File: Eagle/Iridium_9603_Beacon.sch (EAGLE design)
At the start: 100 parts, among them CON4 uFL, J1 SS4-10-3.50-X-D, Q1 DMG3415U-7, Q2 DMG3415U-7, Q3 DMG3415U-7, Q4 DMG3415U-7, Q5 2N2222, U1 MCP111T-240E/TT, U2 SPX3819-3.3, U3 LTC3225EDDB#TRMPBF, U4 MPL3115A2LGA8, U5 ATSAMD21G18_QFN, U6 MAX-M8, U7 LT1634-1,25BMCMS8, X1 32.768

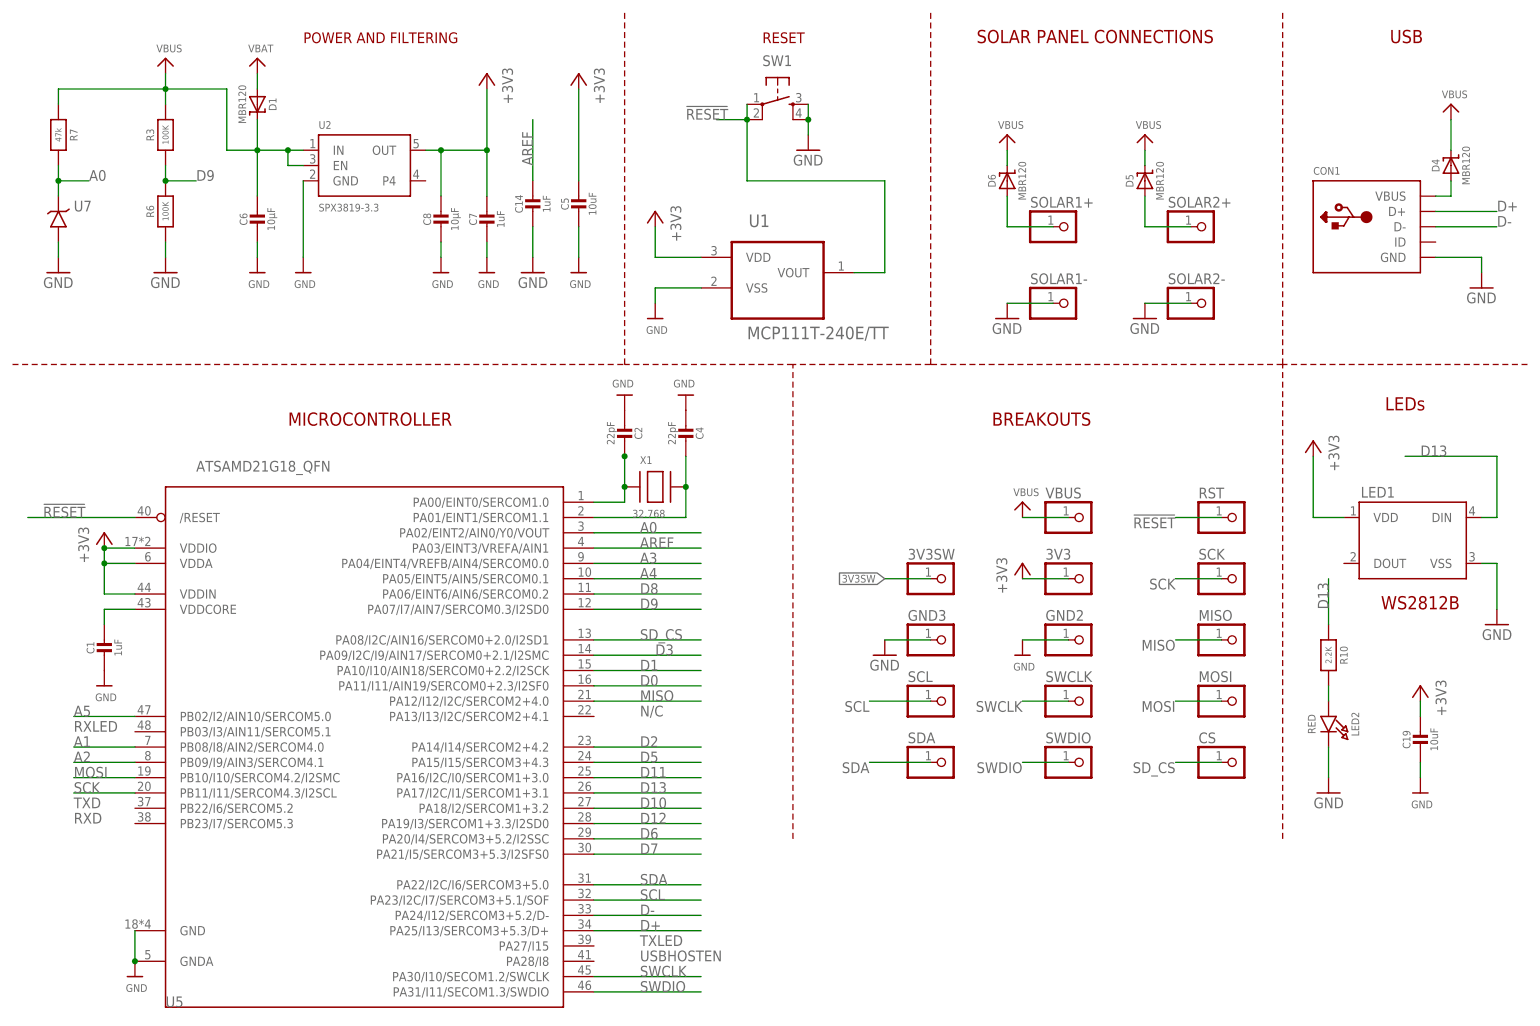
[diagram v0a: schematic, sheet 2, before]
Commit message: Corrected the zero width polygons
Corrected the zero width polygons in the micro USB connector that were causing problems for OSH Park. Thanks go to Paul Loewen @ usask.ca
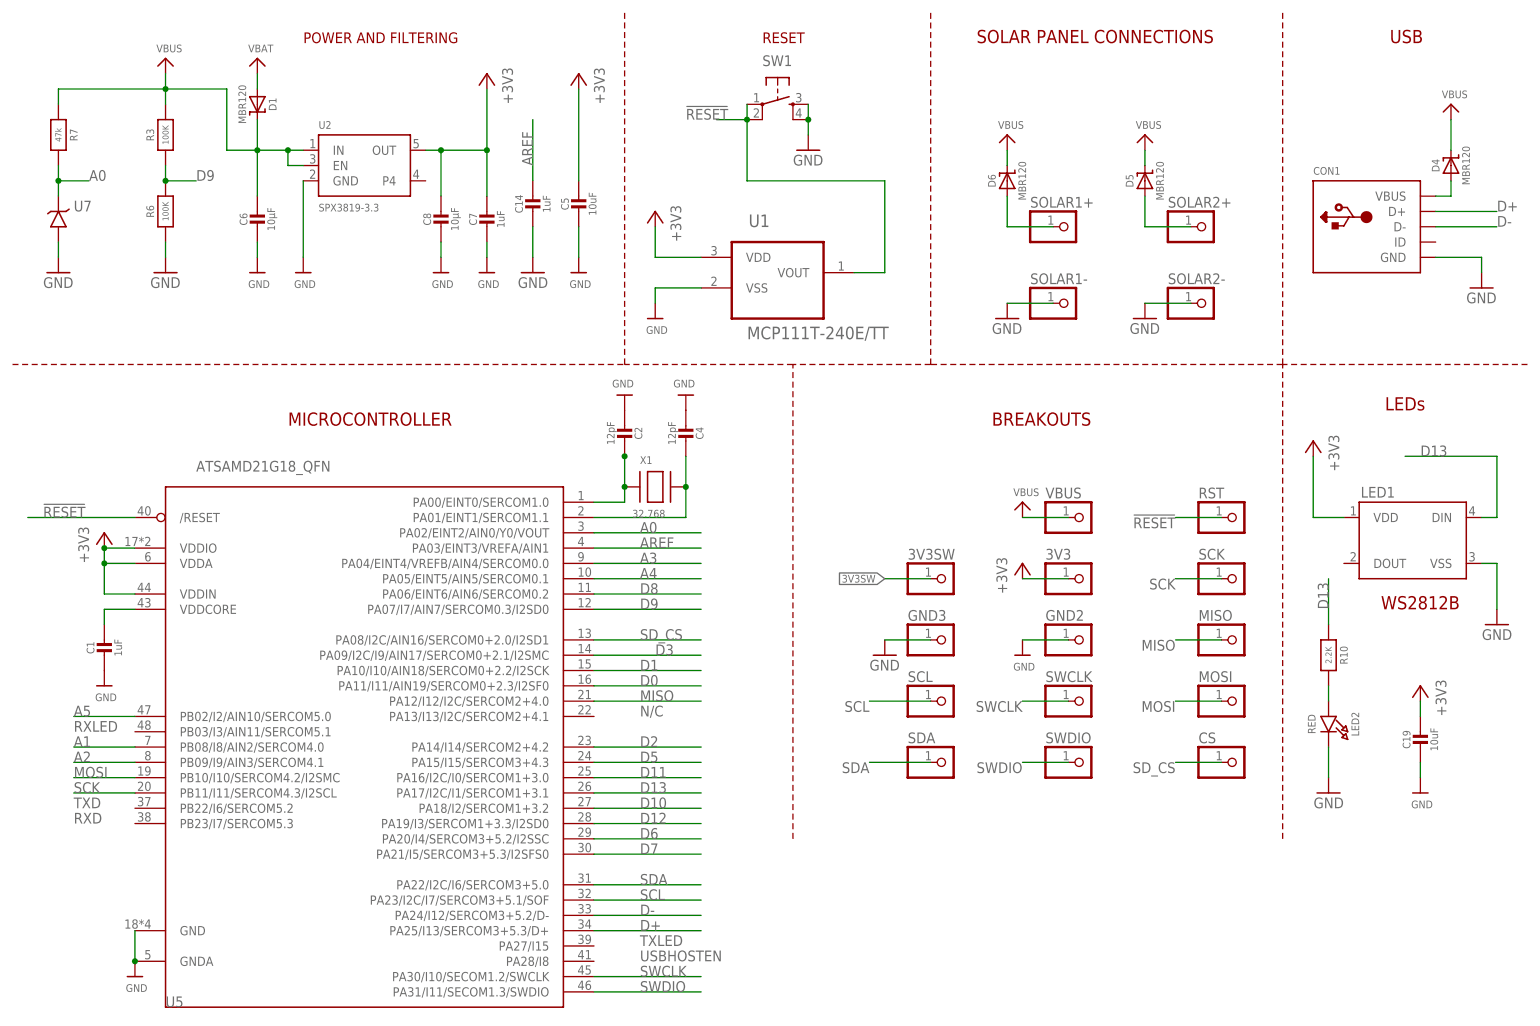
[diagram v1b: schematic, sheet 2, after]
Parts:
- C2, C4: value 22pF -> 12pF
- CON1: device microbuilder:USBFCI_10103594 -> Iridium_9603_Beacon:MICROBUILDER_USBFCI_10103594_CORRECTED
